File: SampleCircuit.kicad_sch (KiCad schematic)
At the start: 46 parts, among them J1 24V INPUT, J2 12V TEST, J3 5V TEST, J4 3.3V TEST, J5 SPEAKER, U1 LMZM23601SILR, U15 TLV803S, U2 ESP32-S3-WROOM-1, U23 RV-3028-C7, U5 LMZM23601SILR, U5 NS4168, U6 LMZM23601SILR, U6 MicroSD

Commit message: Fix duplicate component references: C1, C2, C11, U5, U6
Renumbered second instances to avoid annotation conflicts:
  C1→C105 (ESP32 10uF), C2→C106 (PSU 10uF), C11→C107 (PSU 680uF),
  U5→U24 (PSU LMZM23601), U6→U25 (PSU LMZM23601)

Co-Authored-By: Claude Opus 4.6 <noreply@anthropic.com>
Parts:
- renumbered C1 to C105, C2 to C106, C11 to C107, U5 to U24, U6 to U25
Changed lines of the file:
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@@
 		(on_board yes)
 		(dnp no)
-		(property "Reference" "C1"
+		(property "Reference" "C105"
 			(at 50.8 116.586 0)
 			(effects
@@
 			(project "SampleCircuit"
 				(path "/f1a2b3c4-d5e6-7f89-0a1b-c2d3e4f5a6b7"
-					(reference "C1")
+					(reference "C105")
 					(unit 1)
 				)
@@
 		(on_board yes)
 		(dnp no)
-		(property "Reference" "C11"
+		(property "Reference" "C107"
 			(at 281.94 46.99 0)
 			(effects
@@
 			(project "SampleCircuit"
 				(path "/f1a2b3c4-d5e6-7f89-0a1b-c2d3e4f5a6b7"
-					(reference "C11")
+					(reference "C107")
 					(unit 1)
 				)
@@
 		(on_board yes)
 		(dnp no)
-		(property "Reference" "U5"
+		(property "Reference" "U24"
 			(at 321.31 27.94 0)
 			(effects
@@
 			(project "SampleCircuit"
 				(path "/f1a2b3c4-d5e6-7f89-0a1b-c2d3e4f5a6b7"
-					(reference "U5")
+					(reference "U24")
 					(unit 1)
 				)
@@
 		(on_board yes)
 		(dnp no)
-		(property "Reference" "C2"
+		(property "Reference" "C106"
 			(at 44.48 49.53 0)
 			(effects
@@
 			(project "SampleCircuit"
 				(path "/f1a2b3c4-d5e6-7f89-0a1b-c2d3e4f5a6b7"
-					(reference "C2")
+					(reference "C106")
 					(unit 1)
 				)
@@
 		(on_board yes)
 		(dnp no)
-		(property "Reference" "U6"
+		(property "Reference" "U25"
 			(at 201.31 27.94 0)
 			(effects
@@
 			(project "SampleCircuit"
 				(path "/f1a2b3c4-d5e6-7f89-0a1b-c2d3e4f5a6b7"
-					(reference "U6")
+					(reference "U25")
 					(unit 1)
 				)

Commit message: Revert port pins to power_in for global net connectivity
bidirectional pins don't form global nets in KiCad 9 even with the
(power) flag. power_in is required for net highlighting and ERC
connectivity. The "not driven" ERC warnings are benign.

Co-Authored-By: Claude Opus 4.6 <noreply@anthropic.com>
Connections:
- net +3.3V: now also C11.1
- net GND: now also C11.2, Mem1.6 (SDD0), U2.8 (IO15)
- net SD_CLK: now reaches U2.10 (IO17)
- net SD_CLK: now also Mem1.3 (SCLK), U6.5 (CLK)
- net CS_SD: now reaches U2.11 (IO18)
- net CS_SD: now also U6.2 (DAT3/CD)
- net CS_FLASH: now reaches U2.12 (IO8)
- net CS_FLASH: now also Mem1.2 (CD/SDD3)
- net UD-: now reaches U2.13 (IO19)
- net UD+: now reaches U2.14 (IO20)
- net Enable: now reaches U2.3 (EN)
- net Enable: now also C94.1, R48.2, U15.2 (RESET#)
- net RX: now reaches U2.36 (RXD0)
- net TX: now reaches U2.37 (TXD0)
- net BCLK: now reaches U2.4 (IO4)
- net BCLK: now also U5.3 (BCLK)
- net LRCLK: now reaches U2.5 (IO5)
- net LRCLK: now also U5.2 (LRCLK)
- net DIN: now reaches U2.6 (IO6)
- net DIN: now also U5.4 (SDATA)
- net AMP_EN: now reaches U2.7 (IO7)
- net AMP_EN: now also R20.2, U5.1 (CTRL)
- net SD_MOSI: now reaches U2.9 (IO16)
- net SD_MOSI: now also Mem1.5 (CMD), U6.3 (CMD)
- net SCL: now reaches U23.3 (SCL)
- net SDA: now reaches U23.4 (SDA)
- net OUTN: now reaches U5.5 (VON)
- net OUTN: now also J5.1
- net OUTP: now reaches U5.8 (VOP)
- no-connect marks 41 -> 43

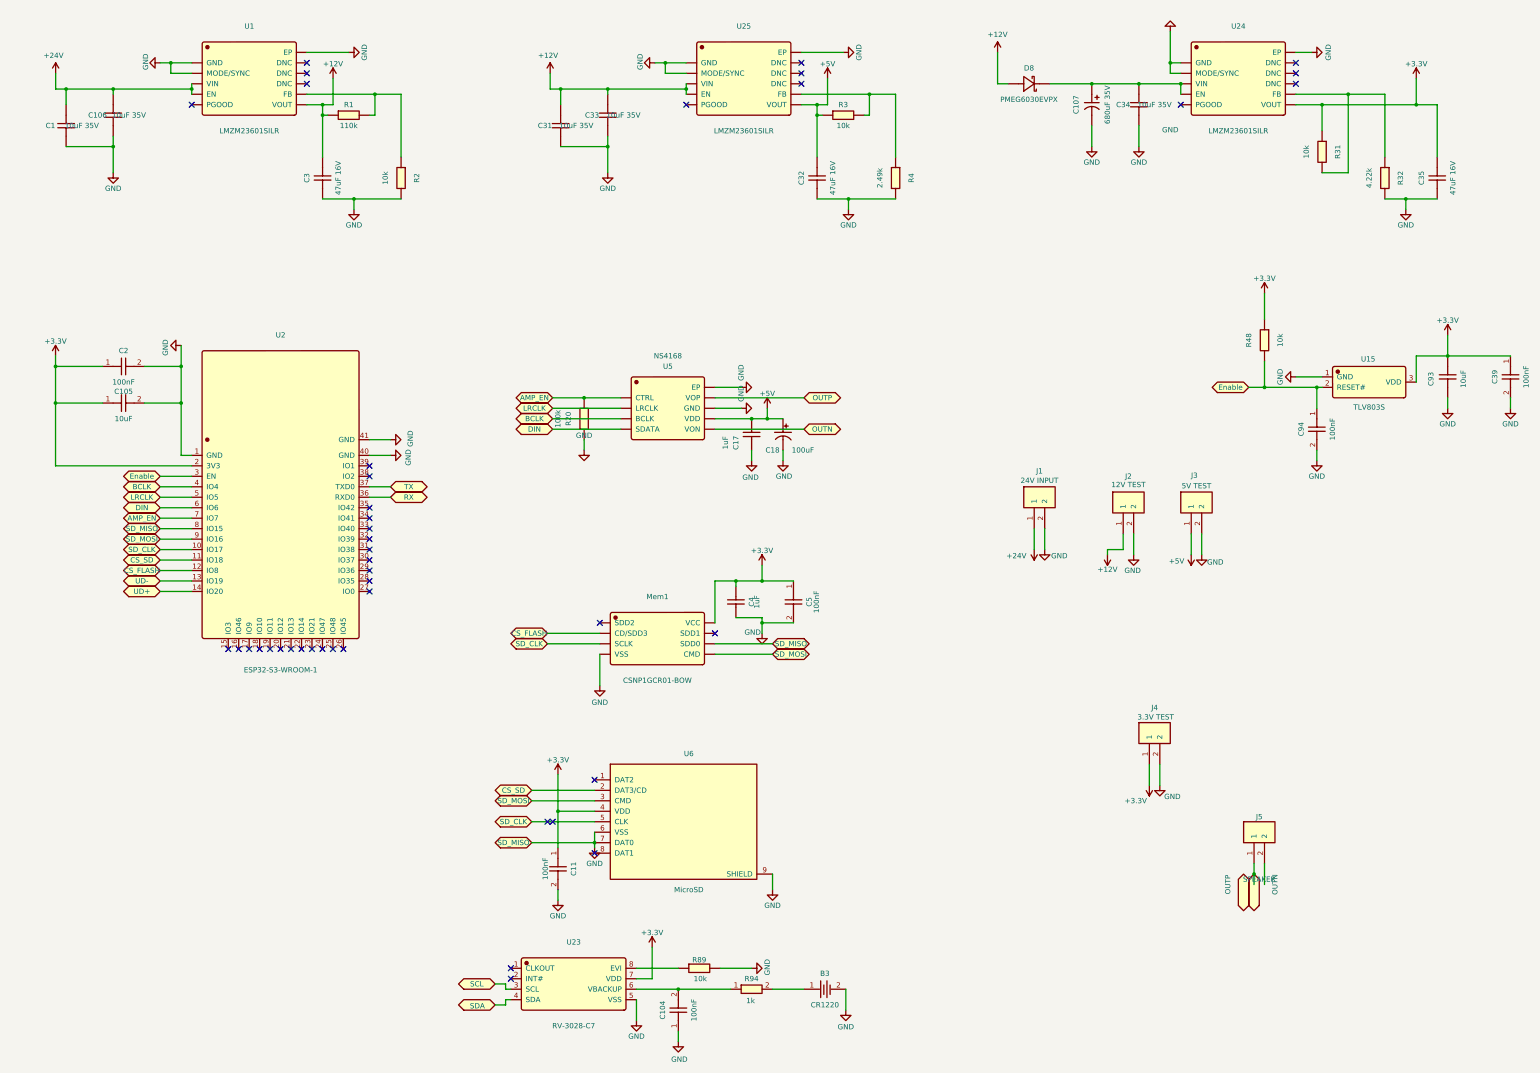
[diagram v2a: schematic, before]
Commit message: Update schematic with RTC/supervisor templates and project settings
Co-Authored-By: Claude Opus 4.6 <noreply@anthropic.com>
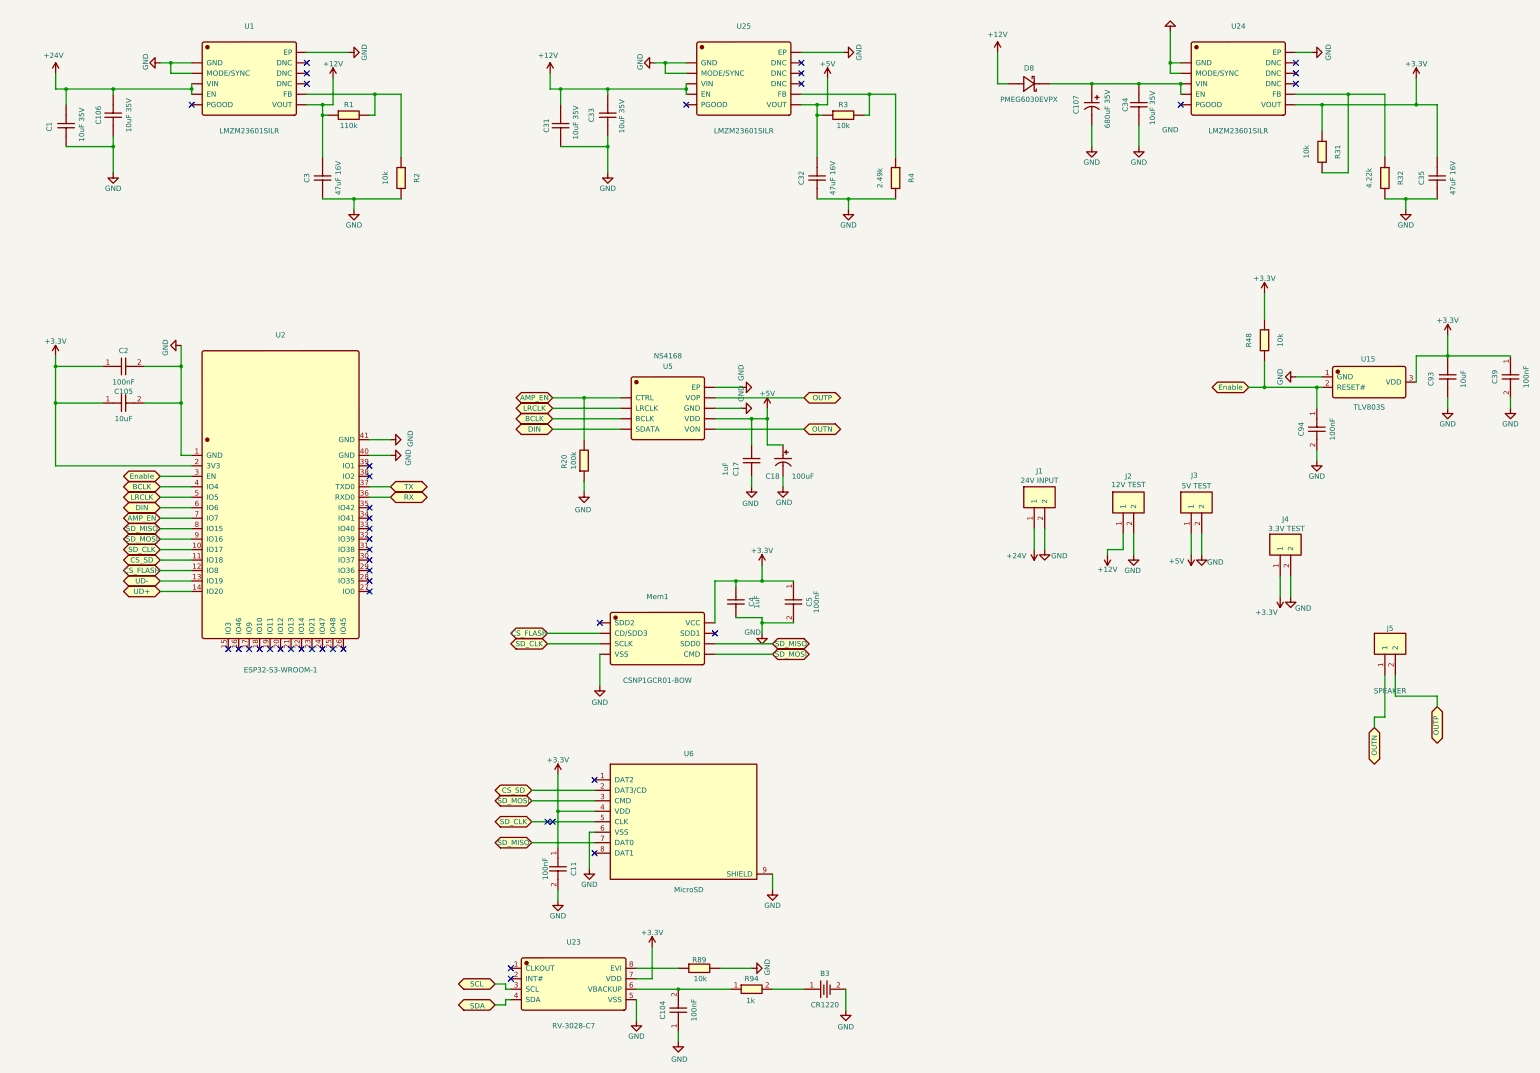
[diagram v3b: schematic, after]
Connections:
- net GND: no longer Mem1.6 (SDD0), U2.8 (IO15), U6.7 (DAT0)
- net OUTP: now also J5.2
- new net SD_MISO: Mem1.6 (SDD0), U2.8 (IO15), U6.7 (DAT0)
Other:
- moved on the sheet: C17, C18, J4, J5, R20

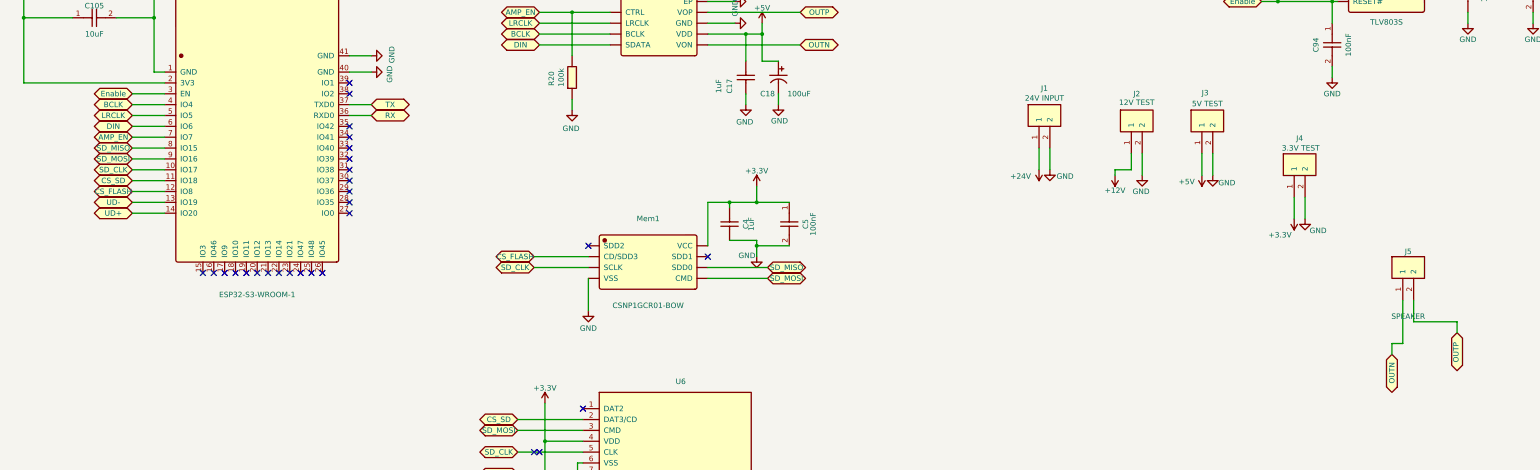
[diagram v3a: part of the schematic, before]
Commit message: Update schematic, symbol library, 12V PSU template, and add patches
Adds SMBJ26CA TVS footprint, updates 12V PSU build script/manifest/spec,
and includes schematic wiring changes and patch files.

Co-Authored-By: Claude Opus 4.6 <noreply@anthropic.com>
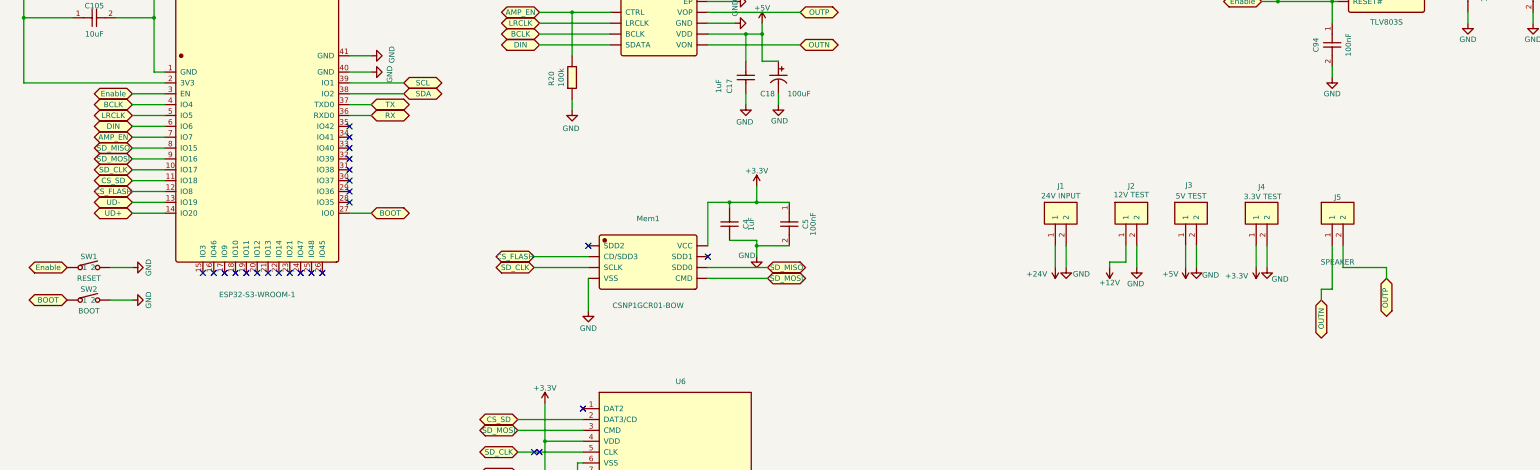
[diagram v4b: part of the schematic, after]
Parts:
- added SW1: RESET, JLCImport:TS665WS_C2686403, symbol JLCImport:TS665WS_C2686403
- added SW2: BOOT, JLCImport:TS665WS_C2686403, symbol JLCImport:TS665WS_C2686403
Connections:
- net Enable: now also SW1.1
- net GND: now also SW1.2, SW2.2
- net SCL: now also U2.39 (IO1)
- net SDA: now also U2.38 (IO2)
- net BOOT: now reaches U2.27 (IO0)
- net BOOT: now also SW2.1
- no-connect marks 43 -> 40
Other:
- moved on the sheet: J1, J2, J3, J4, J5

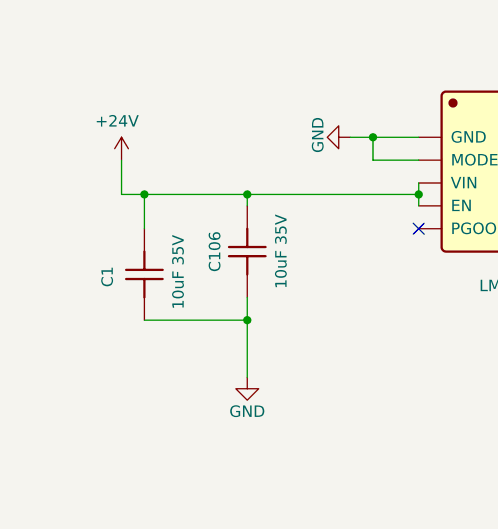
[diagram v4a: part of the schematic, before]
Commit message: Add 24V input protection: D9 (SS34 Schottky) + D10 (SMBJ26CA TVS)
Patches schematic with reverse polarity protection (D9, SS34 3A 40V
series Schottky) and transient voltage suppression (D10, SMBJ26CA
26V bidirectional TVS) on the 24V input rail feeding U1 LMZM23601.

Co-Authored-By: Claude Opus 4.6 <noreply@anthropic.com>
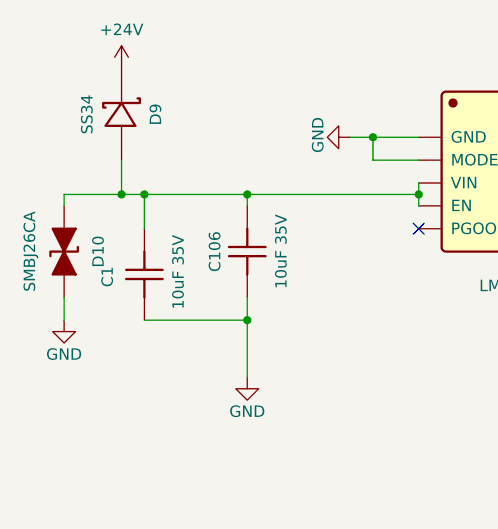
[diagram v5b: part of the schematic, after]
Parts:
- added D10: SMBJ26CA, JLCImport:SMBJ26CA_C89651, symbol JLCImport:SMBJ26CA_C89651
- added D9: SS34, JLCImport:SS34_C8678, symbol JLCImport:SS34_C8678
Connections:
- net +24V: now also D9.1 (K); no longer C1.2, C106.2, U1.3 (VIN), U1.4 (EN)
- net GND: now also D10.2 (A)
- new net: C1.2, C106.2, D10.1 (K), D9.2 (A), U1.3 (VIN), U1.4 (EN)
